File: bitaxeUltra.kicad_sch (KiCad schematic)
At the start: 20 parts, among them J1 54-00164

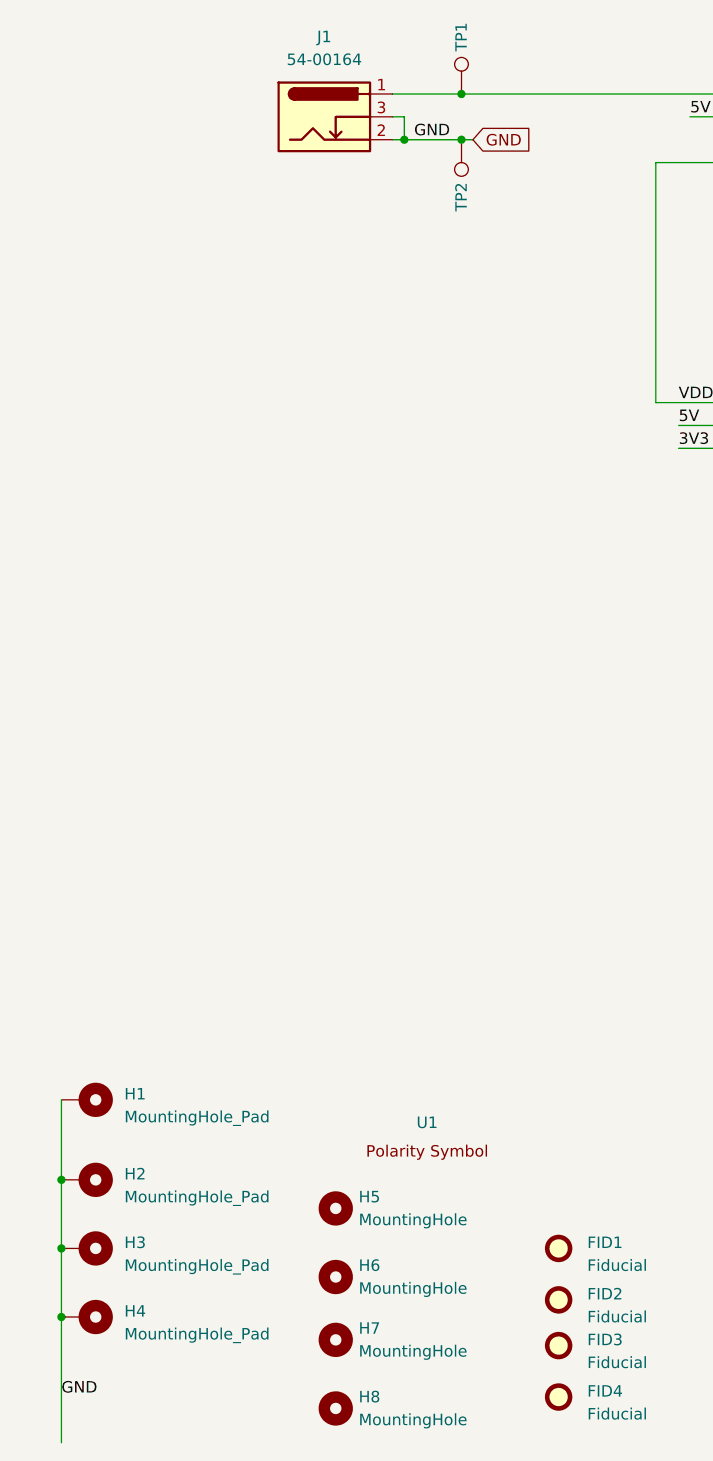
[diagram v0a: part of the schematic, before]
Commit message: use global GND level provided by default with KiCad and remove custom global GND
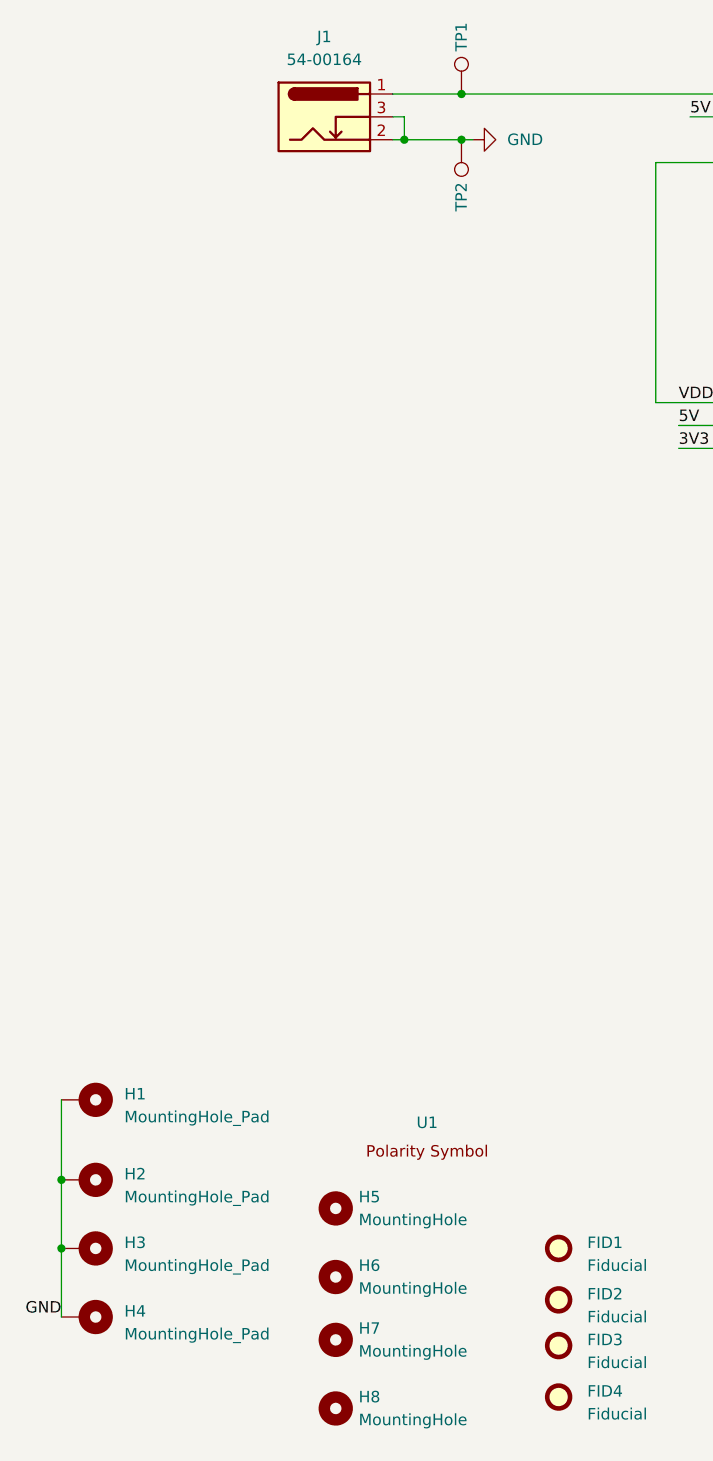
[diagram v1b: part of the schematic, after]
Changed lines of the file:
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@@
 (kicad_sch
-	(version 20231120)
+	(version 20250114)
 	(generator "eeschema")
-	(generator_version "8.0")
+	(generator_version "9.0")
 	(paper "A")
 	(title_block
@@
 	)
 	(junction
-		(at 35.56 179.07)
-		(diameter 0)
-		(color 0 0 0 0)
-	)
-	(junction
 		(at 80.01 43.18)
 		(diameter 0)
@@
 	(wire
 		(pts
-			(xy 35.56 179.07) (xy 35.56 193.04)
-		)
-		(stroke
-			(width 0)
-			(type default)
-		)
-	)
-	(wire
-		(pts
 			(xy 35.56 154.94) (xy 35.56 163.83)
 		)
@@
 	(label "VDD"
 		(at 166.37 83.82 0)
-		(fields_autoplaced yes)
 		(effects
 			(font
@@
 	(label "3V3"
 		(at 104.14 82.55 0)
-		(fields_autoplaced yes)
 		(effects
 			(font
@@
 	(label "RST"
 		(at 166.37 74.93 0)
-		(fields_autoplaced yes)
 		(effects
 			(font
@@
 	(label "VDD"
 		(at 104.14 77.47 0)
-		(fields_autoplaced yes)
 		(effects
 			(font
@@
 	(label "5V"
 		(at 105.41 45.72 0)
-		(fields_autoplaced yes)
 		(effects
 			(font
@@
 	(label "5V"
 		(at 167.64 107.95 0)
-		(fields_autoplaced yes)
 		(effects
 			(font
@@
 	(label "SDA"
 		(at 198.12 69.85 0)
-		(fields_autoplaced yes)
 		(effects
 			(font
@@
 	)
 	(label "GND"
-		(at 35.56 187.96 0)
-		(fields_autoplaced yes)
+		(at 35.56 179.07 180)
 		(effects
 			(font
 				(size 1.27 1.27)
 			)
-			(justify left bottom)
+			(justify right bottom)
 		)
 	)
 	(label "RX"
 		(at 166.37 69.85 0)
-		(fields_autoplaced yes)
 		(effects
 			(font
@@
 	(label "3V3"
 		(at 133.35 44.45 0)
-		(fields_autoplaced yes)
 		(effects
 			(font
@@
 	(label "3V3"
 		(at 166.37 86.36 0)
-		(fields_autoplaced yes)
 		(effects
 			(font
@@
 	(label "SCL"
 		(at 198.12 72.39 0)
-		(fields_autoplaced yes)
 		(effects
 			(font
@@
 	(label "5V"
 		(at 166.37 88.9 0)
-		(fields_autoplaced yes)
 		(effects
 			(font
@@
 	(label "3V3"
 		(at 167.64 110.49 0)
-		(fields_autoplaced yes)
 		(effects
 			(font
@@
 	(label "5V"
 		(at 104.14 80.01 0)
-		(fields_autoplaced yes)
 		(effects
 			(font
@@
 		)
 	)
-	(label "GND"
-		(at 78.74 48.26 180)
-		(fields_autoplaced yes)
+	(label "TX"
+		(at 166.37 72.39 0)
 		(effects
 			(font
 				(size 1.27 1.27)
 			)
-			(justify right bottom)
-		)
-	)
-	(label "TX"
-		(at 166.37 72.39 0)
-		(fields_autoplaced yes)
-		(effects
-			(font
-				(size 1.27 1.27)
-			)
 			(justify left bottom)
-		)
-	)
-	(global_label "GND"
-		(shape input)
-		(at 81.28 48.26 0)
-		(fields_autoplaced yes)
-		(effects
-			(font
-				(size 1.27 1.27)
-			)
-			(justify left)
-		)
-		(property "Intersheetrefs" "${INTERSHEET_REFS}"
-			(at 87.5636 48.1806 0)
-			(effects
-				(font
-					(size 1.27 1.27)
-				)
-				(justify left)
-				(hide yes)
-			)
 		)
 	)
@@
 	)
 	(symbol
+		(lib_id "power:GND")
+		(at 81.28 48.26 90)
+		(unit 1)
+		(exclude_from_sim no)
+		(in_bom yes)
+		(on_board yes)
+		(dnp no)
+		(fields_autoplaced yes)
+		(property "Reference" "#PWR05"
+			(at 87.63 48.26 0)
+			(effects
+				(font
+					(size 1.27 1.27)
+				)
+				(hide yes)
+			)
+		)
+		(property "Value" "GND"
+			(at 85.09 48.2599 90)
+			(effects
+				(font
+					(size 1.27 1.27)
+				)
+				(justify right)
+			)
+		)
+		(property "Footprint" ""
+			(at 81.28 48.26 0)
+			(effects
+				(font
+					(size 1.27 1.27)
+				)
+				(hide yes)
+			)
+		)
+		(property "Datasheet" ""
+			(at 81.28 48.26 0)
+			(effects
+				(font
+					(size 1.27 1.27)
+				)
+				(hide yes)
+			)
+		)
+		(property "Description" "Power symbol creates a global label with name \"GND\" , ground"
+			(at 81.28 48.26 0)
+			(effects
+				(font
+					(size 1.27 1.27)
+				)
+				(hide yes)
+			)
+		)
+		(pin "1"
+		)
+		(instances
+			(project "bitaxeUltra"
+				(path "/e63e39d7-6ac0-4ffd-8aa3-1841a4541b55"
+					(reference "#PWR05")
+					(unit 1)
+				)
+			)
+		)
+	)
+	(symbol
 		(lib_id "Mechanical:Fiducial")
 		(at 109.855 177.8 0)
@@
 		(at 113.03 72.39)
 		(size 17.78 18.034)
+		(exclude_from_sim no)
+		(in_bom yes)
+		(on_board yes)
+		(dnp no)
 		(fields_autoplaced yes)
 		(stroke
@@
 		(at 175.26 99.06)
 		(size 21.59 13.97)
+		(exclude_from_sim no)
+		(in_bom yes)
+		(on_board yes)
+		(dnp no)
 		(fields_autoplaced yes)
 		(stroke
@@
 		(at 113.03 40.64)
 		(size 16.51 20.32)
+		(exclude_from_sim no)
+		(in_bom yes)
+		(on_board yes)
+		(dnp no)
 		(stroke
 			(width 0.1524)
@@
 		(at 175.26 53.34)
 		(size 21.59 38.1)
+		(exclude_from_sim no)
+		(in_bom yes)
+		(on_board yes)
+		(dnp no)
 		(fields_autoplaced yes)
 		(stroke
@@
 		)
 	)
+	(embedded_fonts no)
 )
